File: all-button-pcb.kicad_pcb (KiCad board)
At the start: 2 copper layers, 260 x 150 mm, 22 parts, among them SW1 SW_SPST, SW2 SW_SPST, SW3 SW_SPST, U1 rp2040-zero

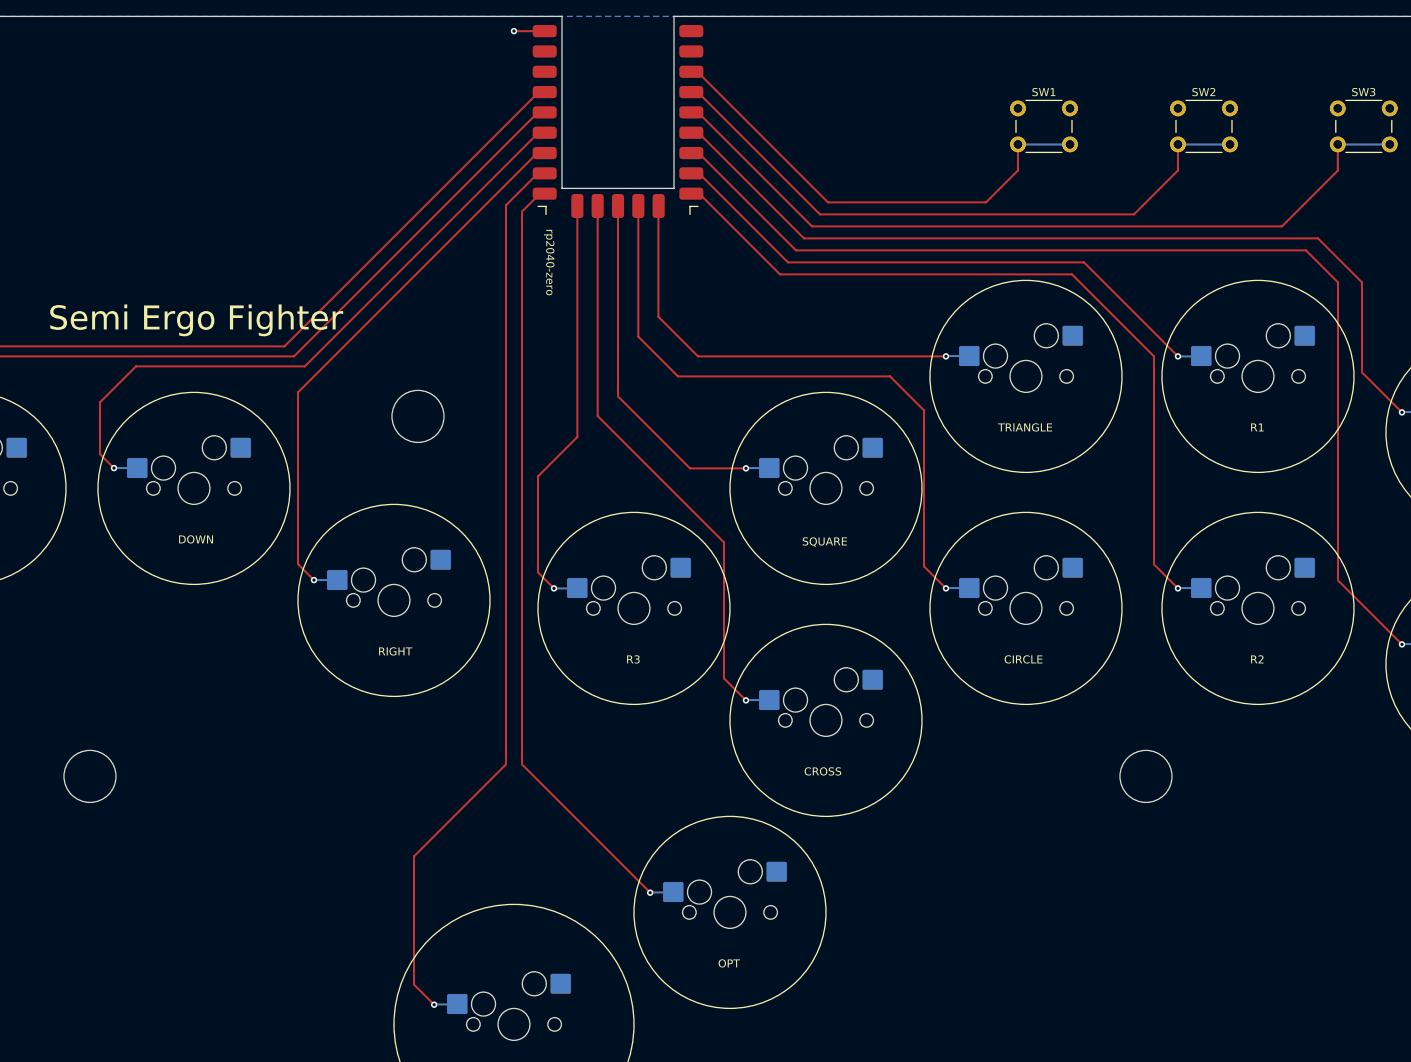
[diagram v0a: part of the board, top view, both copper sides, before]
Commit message: fix gnd pad placement
gnd pad placement swap between 22 and 23
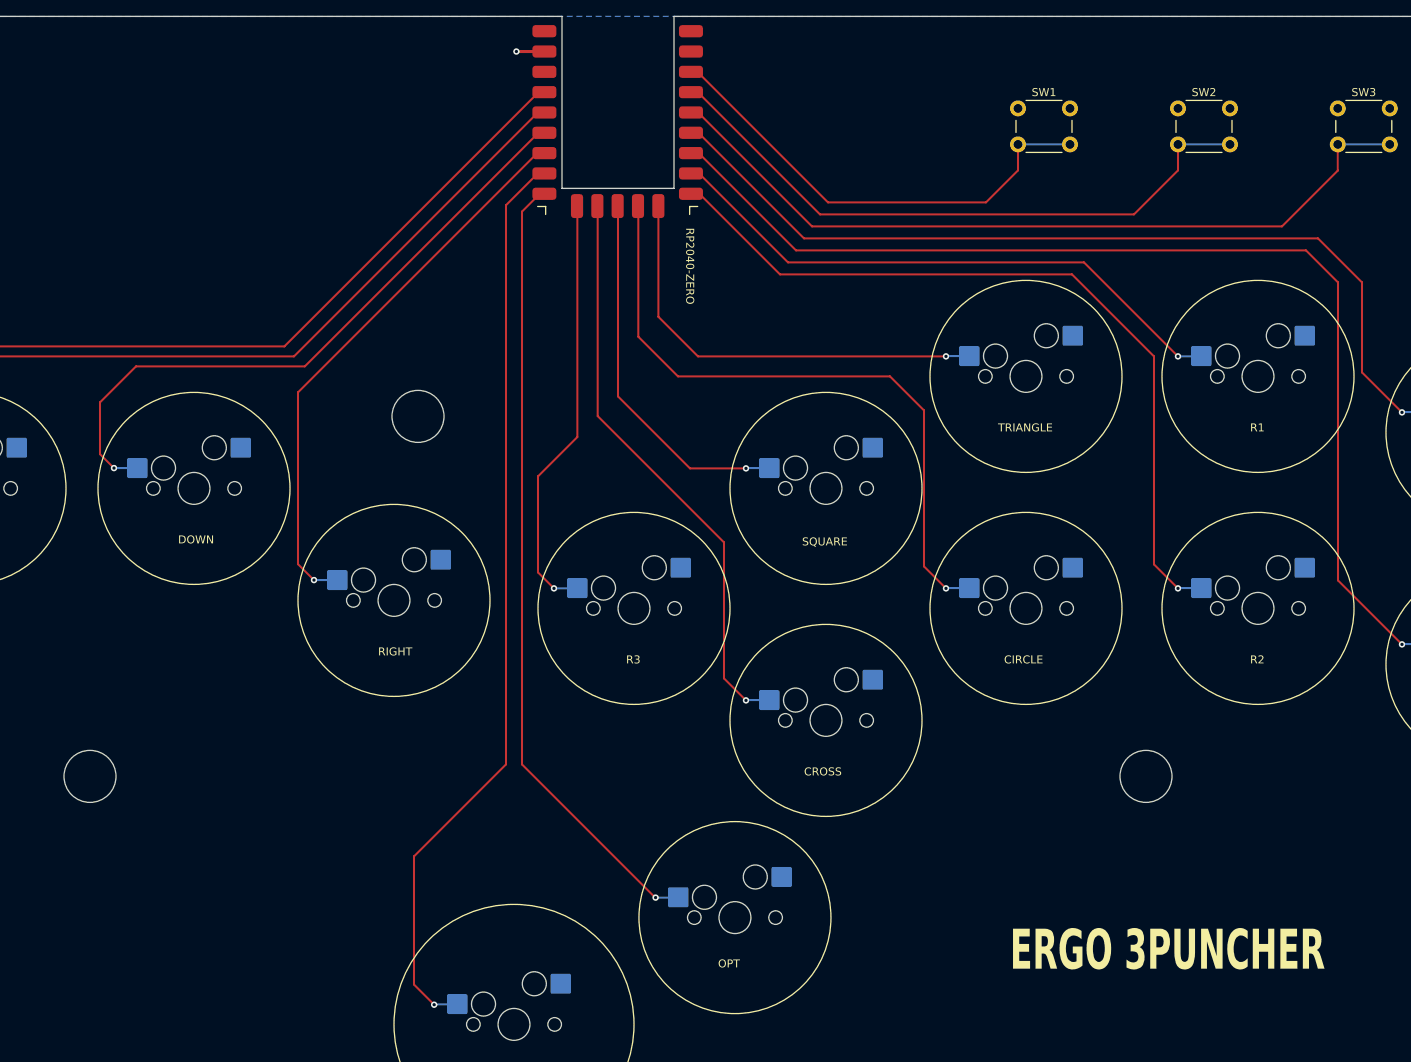
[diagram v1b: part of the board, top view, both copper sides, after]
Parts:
- U1: value rp2040-zero -> RP2040-ZERO
- moved U1 2.51 mm to (212.4, 71.2)
- moved MX8 0.90 mm to (227.1, 174.4)
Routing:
- net OPT5: track 98.5 -> 99.3 mm
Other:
- board text added: "ERGO 3PUNCHER"
- board text removed: "Semi Ergo Fighter"

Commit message: supportive holes
added supportive holes for corners to trim case
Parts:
- added H4: MountingHole, MountingHole:MountingHole_6.5mm, F.Cu at (278.6, 156.8)
- added H5: MountingHole, MountingHole:MountingHole_6.5mm, F.Cu at (89.3, 204.9)
- added H6: MountingHole, MountingHole:MountingHole_6.5mm, F.Cu at (335.7, 204.9)
- U1: value RP2040-ZERO -> rp2040-zero
- moved H2 208.7 mm to (335.7, 68.5)
- moved H3 133.5 mm to (145.2, 149.2)
- moved H1 107.3 mm to (89.3, 68.5)
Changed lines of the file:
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@@
   (net 22 "unconnected-(U1-3V3-Pad21)")
   (net 23 "unconnected-(U1-5V-Pad23)")
+  (footprint "MountingHole:MountingHole_6.5mm" (layer "F.Cu")
+    (at 89.3 204.95)
+    (descr "Mounting Hole 6.5mm, no annular")
+    (tags "mounting hole 6.5mm no annular")
+    (property "Sheetfile" "all-button-pcb.kicad_sch")
+    (property "Sheetname" "")
+    (property "ki_description" "Mounting Hole without connection")
+    (property "ki_keywords" "mounting hole")
+    (attr exclude_from_pos_files)
+    (fp_text reference "H5" (at 0 -7.5) (layer "F.SilkS")
+        (effects (font (size 1 1) (thickness 0.15)))
+    )
+    (fp_text value "MountingHole" (at 0 7.5) (layer "F.Fab")
+        (effects (font (size 1 1) (thickness 0.15)))
+    )
+    (fp_text user "${REFERENCE}" (at 0 0) (layer "F.Fab")
+        (effects (font (size 1 1) (thickness 0.15)))
+    )
+    (fp_circle (center 0 0) (end 6.5 0)
+      (stroke (width 0.15) (type solid)) (fill none) (layer "Cmts.User"))
+    (fp_circle (center 0 0) (end 6.75 0)
+      (stroke (width 0.05) (type solid)) (fill none) (layer "F.CrtYd"))
+    (pad "" np_thru_hole circle (at 0 0) (size 6.5 6.5) (drill 6.5) (layers "*.Cu" "*.Mask"))
+  )
   (footprint "MX_Hotswap:MX-Hotswap-1U-24mm" (layer "F.Cu")
     (at 184.5 134.75)
@@
   )
   (footprint "MountingHole:MountingHole_6.5mm" (layer "F.Cu")
-    (at 278.5 156.75)
+    (at 145.2 149.2)
     (descr "Mounting Hole 6.5mm, no annular")
     (tags "mounting hole 6.5mm no annular")
@@
   )
   (footprint "MountingHole:MountingHole_6.5mm" (layer "F.Cu")
-    (at 187.5 111.75)
+    (at 89.3 68.55)
     (descr "Mounting Hole 6.5mm, no annular")
     (tags "mounting hole 6.5mm no annular")
@@
     )
   )
+  (footprint "MountingHole:MountingHole_6.5mm" (layer "F.Cu")
+    (at 278.55 156.8)
+    (descr "Mounting Hole 6.5mm, no annular")
+    (tags "mounting hole 6.5mm no annular")
+    (property "Sheetfile" "all-button-pcb.kicad_sch")
+    (property "Sheetname" "")
+    (property "ki_description" "Mounting Hole without connection")
+    (property "ki_keywords" "mounting hole")
+    (attr exclude_from_pos_files)
+    (fp_text reference "H4" (at 0 -7.5) (layer "F.SilkS")
+        (effects (font (size 1 1) (thickness 0.15)))
+    )
+    (fp_text value "MountingHole" (at 0 7.5) (layer "F.Fab")
+        (effects (font (size 1 1) (thickness 0.15)))
+    )
+    (fp_text user "${REFERENCE}" (at 0 0) (layer "F.Fab")
+        (effects (font (size 1 1) (thickness 0.15)))
+    )
+    (fp_circle (center 0 0) (end 6.5 0)
+      (stroke (width 0.15) (type solid)) (fill none) (layer "Cmts.User"))
+    (fp_circle (center 0 0) (end 6.75 0)
+      (stroke (width 0.05) (type solid)) (fill none) (layer "F.CrtYd"))
+    (pad "" np_thru_hole circle (at 0 0) (size 6.5 6.5) (drill 6.5) (layers "*.Cu" "*.Mask"))
+  )
   (footprint "MX_Hotswap:MX-Hotswap-1U-24mm" (layer "F.Cu")
     (at 238.5 120.75)
@@
         (effects (font (size 1 1) (thickness 0.15)))
     )
-    (fp_text value "RP2040-ZERO" (at 9.0694 21.7186 -90 unlocked) (layer "F.SilkS")
+    (fp_text value "rp2040-zero" (at 9.0694 21.7186 -90 unlocked) (layer "F.SilkS")
         (effects (font (size 1 1) (thickness 0.15)))
     )
@@
       (net 2 "GND") (pinfunction "ROW") (pintype "passive"))
   )
+  (footprint "MountingHole:MountingHole_6.5mm" (layer "F.Cu")
+    (at 335.7 204.95)
+    (descr "Mounting Hole 6.5mm, no annular")
+    (tags "mounting hole 6.5mm no annular")
+    (property "Sheetfile" "all-button-pcb.kicad_sch")
+    (property "Sheetname" "")
+    (property "ki_description" "Mounting Hole without connection")
+    (property "ki_keywords" "mounting hole")
+    (attr exclude_from_pos_files)
+    (fp_text reference "H6" (at 0 -7.5) (layer "F.SilkS")
+        (effects (font (size 1 1) (thickness 0.15)))
+    )
+    (fp_text value "MountingHole" (at 0 7.5) (layer "F.Fab")
+        (effects (font (size 1 1) (thickness 0.15)))
+    )
+    (fp_text user "${REFERENCE}" (at 0 0) (layer "F.Fab")
+        (effects (font (size 1 1) (thickness 0.15)))
+    )
+    (fp_circle (center 0 0) (end 6.5 0)
+      (stroke (width 0.15) (type solid)) (fill none) (layer "Cmts.User"))
+    (fp_circle (center 0 0) (end 6.75 0)
+      (stroke (width 0.05) (type solid)) (fill none) (layer "F.CrtYd"))
+    (pad "" np_thru_hole circle (at 0 0) (size 6.5 6.5) (drill 6.5) (layers "*.Cu" "*.Mask"))
+  )
   (footprint "MX_Hotswap:MX-Hotswap-1U-24mm" (layer "F.Cu")
     (at 227.12 174.4)
@@
   )
   (footprint "MountingHole:MountingHole_6.5mm" (layer "F.Cu")
-    (at 146.5 156.75)
+    (at 335.7 68.55)
     (descr "Mounting Hole 6.5mm, no annular")
     (tags "mounting hole 6.5mm no annular")
